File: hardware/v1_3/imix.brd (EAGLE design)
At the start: 87 x 102.5 mm, 154 parts, among them J2_3_5_AND_6 ARDUINO_R3NO_HOLES, SW1 TAC_SWITCHSMD, SW2 TAC_SWITCHSMD, U1 BQ2423X, U10 ISL29035, U11 FX0S8700CQ, U12 296-12686-1-ND, U13 SIP32401A, U14 SIP32401A, U15 SIP32401A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

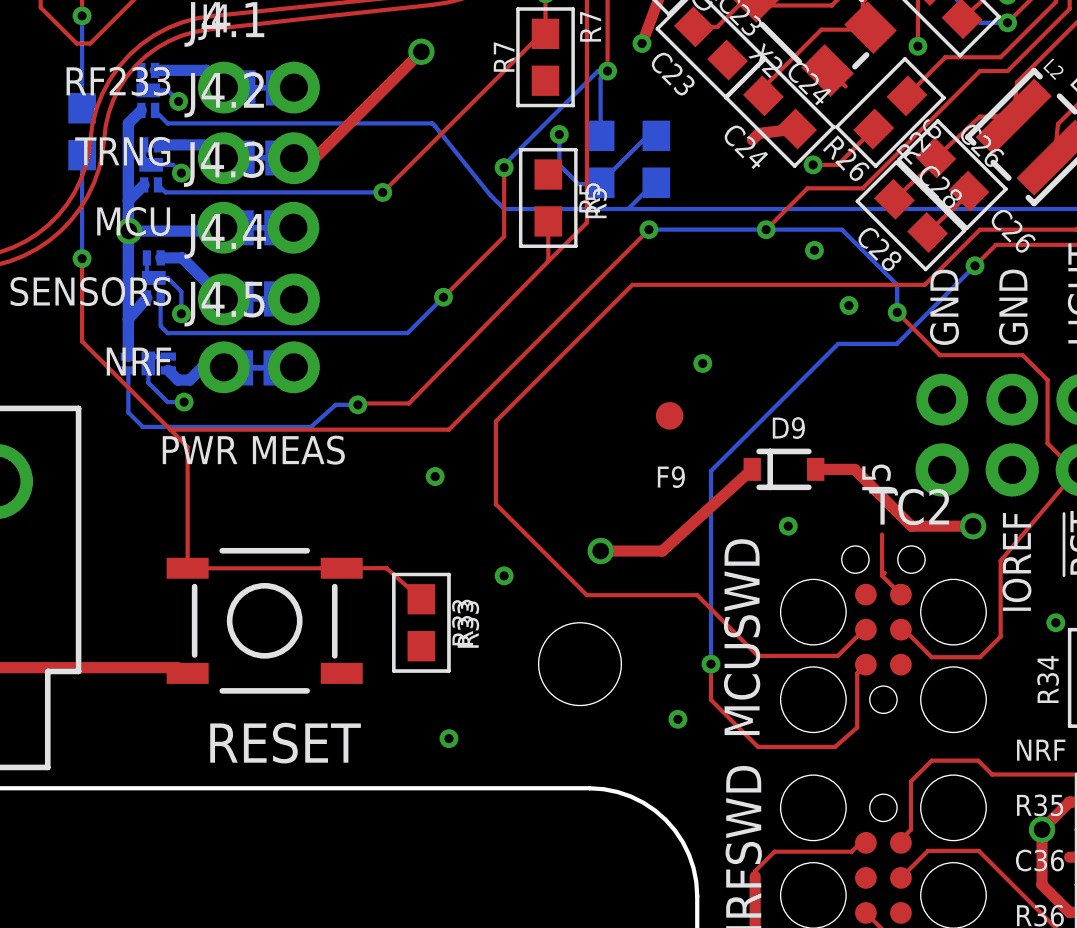
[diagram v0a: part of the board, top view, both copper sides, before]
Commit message: No airwires. Need to run DRC and generate documentation
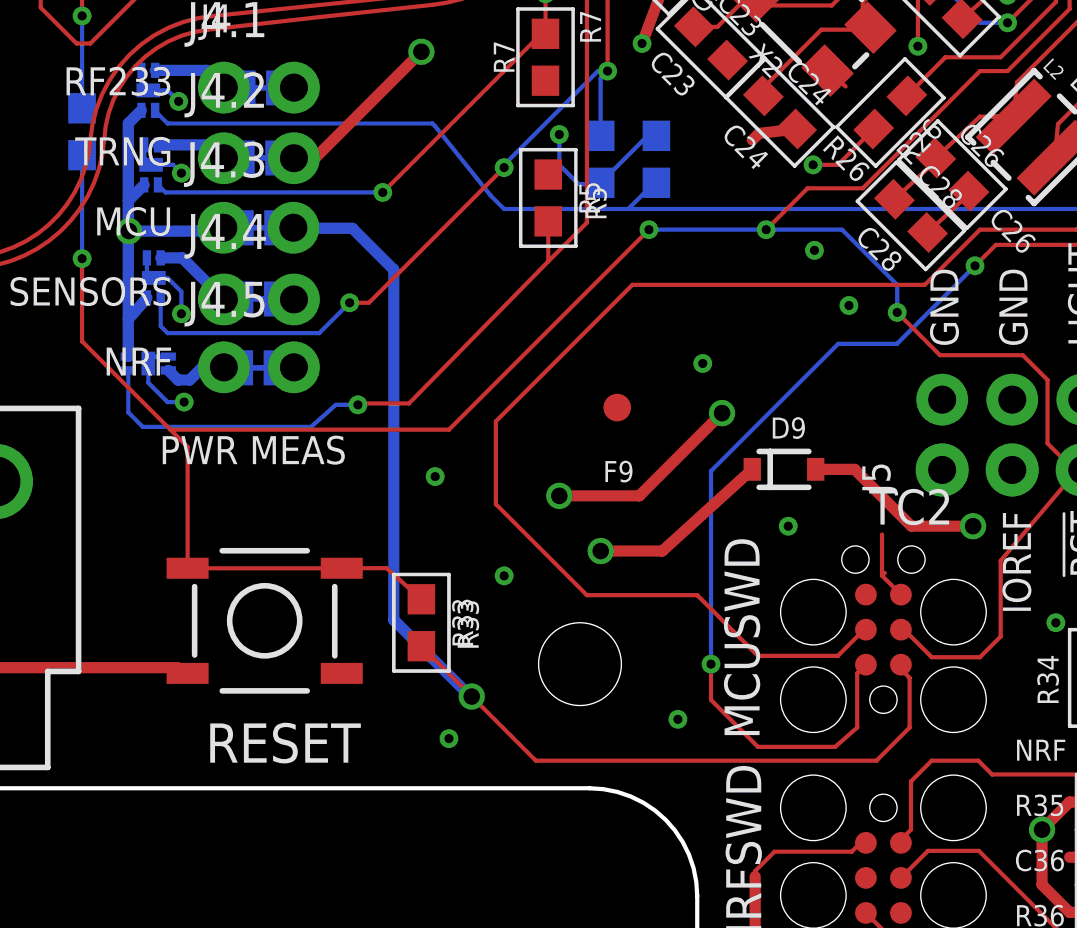
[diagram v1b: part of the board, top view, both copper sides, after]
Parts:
- moved F9 1.92 mm to (34.6, 13.8)
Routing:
- net VCC_MCU_3V3: track 71.0 -> 114.3 mm, vias 14 -> 15
- net VCC_3V3: track 39.4 -> 46.5 mm, vias 3 -> 5
- net SENSE_PWR_EN: track 148.8 -> 147.3 mm
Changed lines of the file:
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@@
 <wire x1="22.2" y1="13" x2="22.5" y2="13" width="0.1524" layer="22" style="shortdash"/>
 <wire x1="21.3" y1="13" x2="21.7" y2="13" width="0.1524" layer="22" style="shortdash"/>
-<text x="35.98" y="10.9" size="0.762" layer="21" font="vector" ratio="12">F9</text>
+<text x="34.08" y="11.1" size="0.762" layer="21" font="vector" ratio="12">F9</text>
 <text x="72.48" y="-9.1" size="0.762" layer="21" font="vector" ratio="12">F10</text>
 <text x="40.48" y="69.9" size="0.762" layer="21" font="vector" ratio="12">F7</text>
@@
 <element name="F7" library="imix" package="FIDUCIAL" value="FIDUCIAL" x="41" y="72.5"/>
 <element name="F8" library="imix" package="FIDUCIAL" value="FIDUCIAL" x="65.2" y="65.9"/>
-<element name="F9" library="imix" package="FIDUCIAL" value="FIDUCIAL" x="36.5" y="13.5"/>
+<element name="F9" library="imix" package="FIDUCIAL" value="FIDUCIAL" x="34.6" y="13.8"/>
 <element name="F10" library="imix" package="FIDUCIAL" value="FIDUCIAL" x="73.5" y="-6.5"/>
 <element name="R4" library="imix" package="0603-RES" value="10K" x="34" y="22.8" rot="MR90"/>
@@
 <wire x1="42.6" y1="22.6" x2="41.7" y2="22.6" width="0.1524" layer="1"/>
 <via x="41.7" y="22.6" extent="1-16" drill="0.3302"/>
-<wire x1="27.5" y1="5.15" x2="44.885" y2="4.48" width="0" layer="19" extent="1-1"/>
-<wire x1="22.86" y1="20.32" x2="27.5" y2="5.15" width="0" layer="19" extent="1-15"/>
+<wire x1="27.5" y1="5.15" x2="29.325" y2="3.325" width="0.1524" layer="1"/>
+<wire x1="29.325" y1="3.325" x2="31.65" y2="1" width="0.1524" layer="1"/>
+<wire x1="31.65" y1="1" x2="44" y2="1" width="0.1524" layer="1"/>
+<wire x1="44" y1="1" x2="45.2" y2="2.2" width="0.1524" layer="1"/>
+<wire x1="45.2" y1="2.2" x2="45.2" y2="4" width="0.1524" layer="1"/>
+<wire x1="45.2" y1="4" x2="44.885" y2="4.315" width="0.1524" layer="1"/>
+<wire x1="44.885" y1="4.315" x2="44.885" y2="4.48" width="0.1524" layer="1"/>
+<wire x1="22.86" y1="20.32" x2="22.88" y2="20.3" width="0.4064" layer="16"/>
+<wire x1="22.88" y1="20.3" x2="25" y2="20.3" width="0.4064" layer="16"/>
+<wire x1="25" y1="20.3" x2="26.5" y2="18.8" width="0.4064" layer="16"/>
+<wire x1="26.5" y1="18.8" x2="26.5" y2="6.1" width="0.4064" layer="16"/>
+<wire x1="26.5" y1="6.1" x2="29.275" y2="3.325" width="0.4064" layer="16"/>
+<wire x1="29.275" y1="3.325" x2="29.325" y2="3.325" width="0.4064" layer="16"/>
+<via x="29.325" y="3.325" extent="1-16" drill="0.6"/>
 </signal>
 <signal name="USART3_RTS">
@@
 <wire x1="75.1" y1="-5.2" x2="76.1" y2="-5.2" width="0.1524" layer="16"/>
 <wire x1="22.88" y1="17.72" x2="24.6" y2="16" width="0.4064" layer="15"/>
-<wire x1="24.6" y1="16" x2="33.8" y2="16" width="0.4064" layer="15"/>
-<wire x1="33.8" y1="16" x2="39.5" y2="10.3" width="0.4064" layer="15"/>
-<wire x1="39.5" y1="10.3" x2="45.2" y2="10.3" width="0.4064" layer="15"/>
+<wire x1="24.6" y1="16" x2="32.9" y2="16" width="0.4064" layer="15"/>
+<wire x1="32.9" y1="16" x2="38.6" y2="10.3" width="0.4064" layer="15"/>
+<wire x1="38.6" y1="10.3" x2="45.2" y2="10.3" width="0.4064" layer="15"/>
 <wire x1="45.2" y1="10.3" x2="47.4" y2="8.1" width="0.4064" layer="15"/>
 <wire x1="47.4" y1="8.1" x2="68.9" y2="8.1" width="0.4064" layer="15"/>
@@
 <contactref element="U18" pad="6"/>
 <contactref element="U18" pad="12"/>
-<wire x1="30.5" y1="22.5" x2="30.5" y2="20" width="0.1524" layer="1"/>
-<wire x1="30.5" y1="20" x2="28.3" y2="17.8" width="0.1524" layer="1"/>
 <wire x1="34.25" y1="26" x2="34" y2="25.75" width="0.1524" layer="16"/>
 <wire x1="34" y1="25.75" x2="34" y2="23.65" width="0.1524" layer="16"/>
-<wire x1="18.3" y1="16.5" x2="27" y2="16.5" width="0.1524" layer="16"/>
-<wire x1="27" y1="16.5" x2="28.3" y2="17.8" width="0.1524" layer="16"/>
-<via x="28.3" y="17.8" extent="1-16" drill="0.3302"/>
+<via x="24.9" y="17.6" extent="1-16" drill="0.3302"/>
 <wire x1="69" y1="43.5" x2="78.6" y2="43.5" width="0.1524" layer="16"/>
 <wire x1="78.6" y1="43.5" x2="79.6" y2="42.5" width="0.1524" layer="16"/>
@@
 <wire x1="18.05" y1="17.775" x2="18.05" y2="16.75" width="0.1524" layer="16"/>
 <wire x1="18.05" y1="16.75" x2="18.3" y2="16.5" width="0.1524" layer="16"/>
+<wire x1="24.9" y1="17.6" x2="23.8" y2="16.5" width="0.1524" layer="16"/>
+<wire x1="23.8" y1="16.5" x2="18.3" y2="16.5" width="0.1524" layer="16"/>
+<wire x1="30.5" y1="22.5" x2="25.6" y2="17.6" width="0.1524" layer="1"/>
+<wire x1="25.6" y1="17.6" x2="24.9" y2="17.6" width="0.1524" layer="1"/>
 </signal>
 <signal name="VCC_3V3" class="1">
@@
 <wire x1="16.875" y1="20.2" x2="16.9" y2="20.2" width="0.4064" layer="16"/>
 <via x="16.9" y="20.2" extent="1-16" drill="0.6"/>
-<wire x1="21.102" y1="20.32" x2="48.92" y2="11.54" width="0" layer="19" extent="16-16"/>
+<via x="38.4" y="13.6" extent="1-16" drill="0.6"/>
+<wire x1="38.4" y1="13.6" x2="35.4" y2="10.6" width="0.4064" layer="1"/>
+<wire x1="35.4" y1="10.6" x2="32.5" y2="10.6" width="0.4064" layer="1"/>
+<via x="32.5" y="10.6" extent="1-16" drill="0.6"/>
 </signal>
 <signal name="VCC_EXT_5V" class="1">

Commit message: Passes DRC
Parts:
- C47, C48: device imix:C0603 -> imix:C0603-NOSILK
- moved C6 0.55 mm to (54.4, 74.2)
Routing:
- net GND: track 234.7 -> 228.7 mm
- net VCC_3V3: track 46.5 -> 47.4 mm
- net N$4: track 10.3 -> 10.8 mm

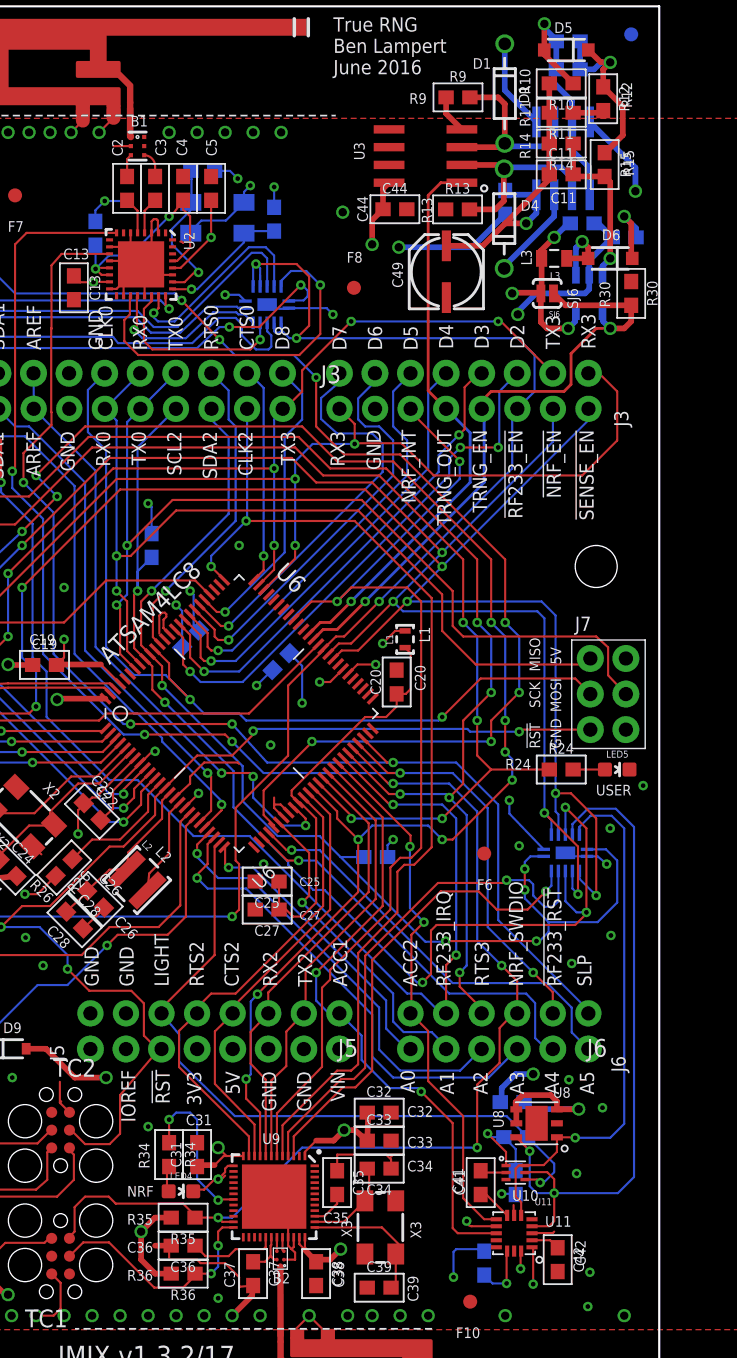
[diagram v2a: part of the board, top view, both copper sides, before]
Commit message: Rearranged analog pins according to #16
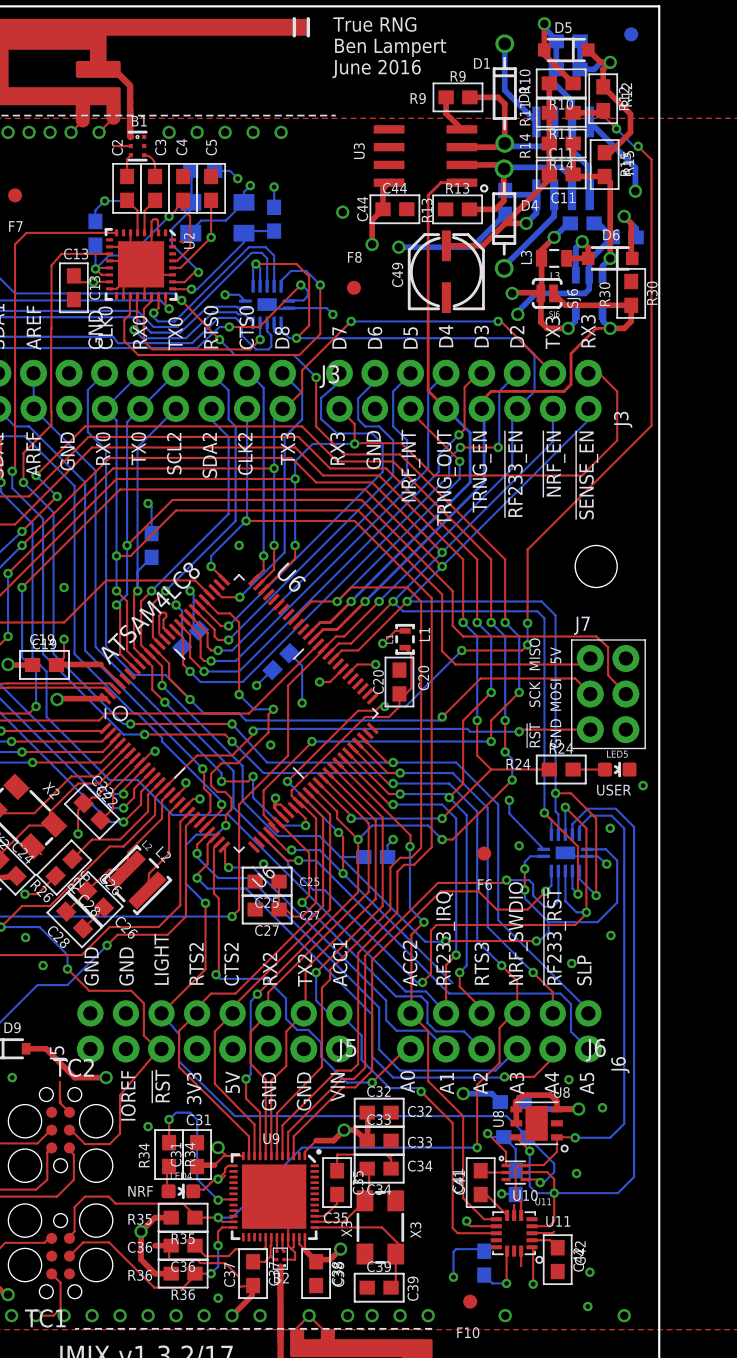
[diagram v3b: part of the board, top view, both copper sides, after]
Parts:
- moved C20 0.20 mm to (68.5, 37.8)
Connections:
- net ADCIFE0: now also U6.24; no longer U6.25
- net ADCIFE1: now also U6.25; no longer U6.31
- net ADCIFE2: now also U6.31; no longer U6.22
- net ADCIFE3: now also U6.22; no longer U6.23
- net ADCIFE4: now also U6.23; no longer U6.28
- net ADCIFE5: now also U6.28; no longer U6.29
- net GPIO8: now also U6.78; no longer U6.80
- net LIGHT_!INT: now also U6.80; no longer U6.24
- net VHIGHSAMPLE: now also U6.29
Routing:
- net VHIGHSAMPLE: track 2.21 -> 92.6 mm, vias 0 -> 10
- net LIGHT_!INT: track 50.7 -> 77.2 mm, vias 1 -> 5
- net ADCIFE4: track 28.4 -> 37.7 mm, vias 1 -> 2
- net ADCIFE0: track 21.1 -> 29.3 mm, vias 1 -> 2
- net ADCIFE2: track 31.2 -> 24.8 mm
- net GND: track 228.7 -> 225.4 mm, vias 94 -> 95
- net GPIO8: track 21.7 -> 20.5 mm
- net ADCIFE3: track 34.8 -> 33.7 mm
- net USART0_RX: track 64.3 -> 65.1 mm
- net AREF: track 44.2 -> 44.9 mm
- net ADCIFE1: track 22.7 -> 23.3 mm

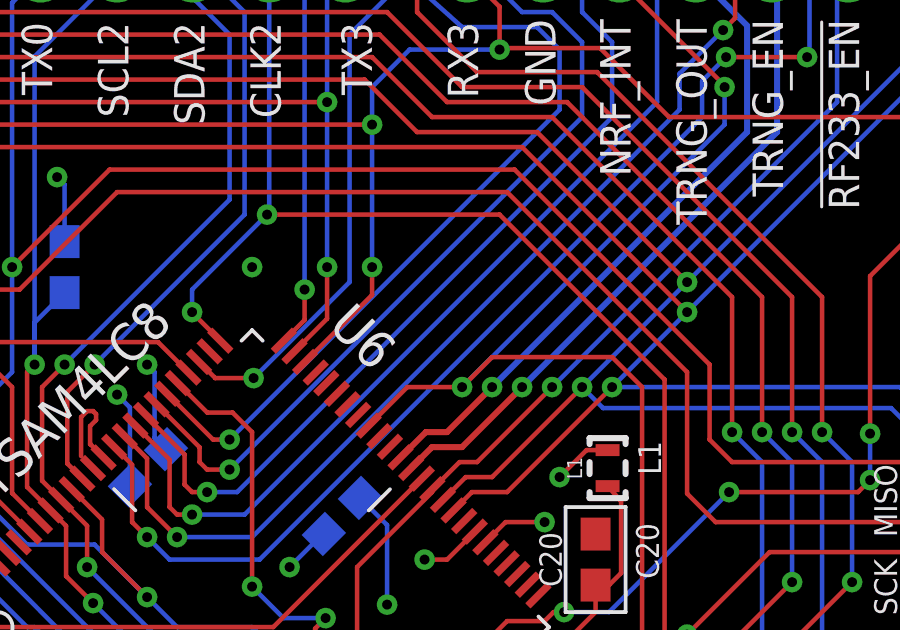
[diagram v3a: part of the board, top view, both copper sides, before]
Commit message: Fab/assembly documentation for v1.3
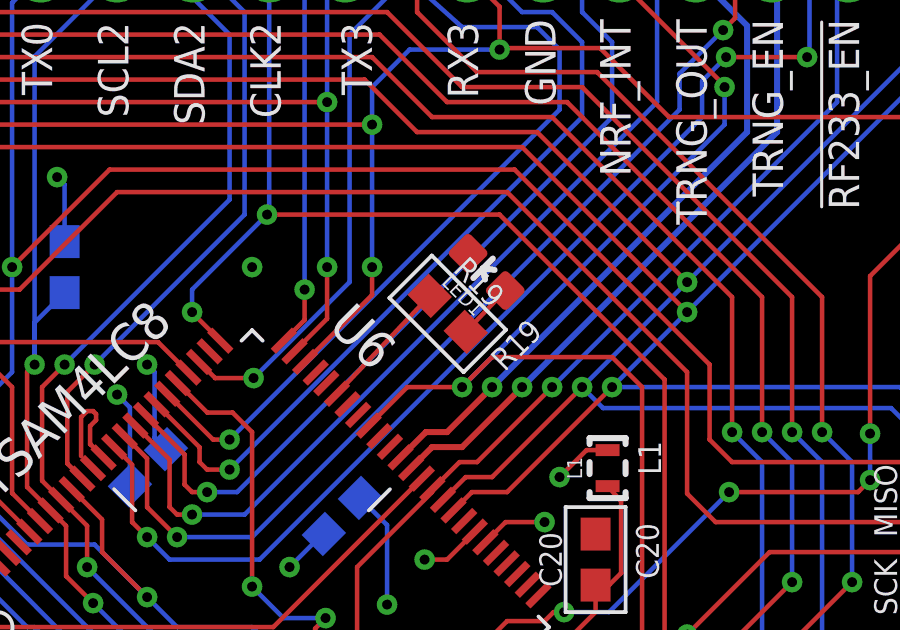
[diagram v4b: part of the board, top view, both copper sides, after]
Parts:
- added LED1: (no value), imix:LED-0603
- added R19: 1K, imix:0603-RES
- LED2, LED3, LED4, LED5: value BLUE -> (none)
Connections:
- new net KERNEL_LED: R19.1, U6.70
- new net N$14: LED1.A, R19.2
- net GND: now also LED1.C
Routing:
- net KERNEL_LED: track 0.00 -> 4.50 mm
- net N$14: track 0.00 -> 1.91 mm
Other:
- board text added: "R19"
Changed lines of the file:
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@@
 <text x="59.4" y="-5.2" size="0.762" layer="21" font="vector" ratio="12">B2</text>
 <wire x1="8" y1="7.3" x2="11" y2="7.3" width="0.4064" layer="21"/>
+<text x="65.42020625" y="43.985353125" size="0.762" layer="21" font="vector" ratio="12" rot="R45">R19</text>
 </plain>
 <attributes>
@@
 <element name="L1" library="imix" package="L0603" value="BLM18HE152SN1" x="69.25" y="40" rot="R90"/>
 <element name="L2" library="imix" package="L1212" value="22uH LQH3NPN220MJ0" x="49.715" y="23.605" rot="R315"/>
-<element name="LED2" library="imix" package="LED-0603" value="BLUE" x="3" y="44.5" smashed="yes" rot="R90">
+<element name="LED2" library="imix" package="LED-0603" value="" x="3" y="44.5" smashed="yes" rot="R90">
 <attribute name="PROD_ID" value="DIO-08575" x="3" y="44.5" size="1.778" layer="27" rot="R90" display="off"/>
 <attribute name="NAME" x="2.989" y="43.4015" size="0.5" layer="25" font="vector" ratio="12" rot="R180" align="center"/>
@@
 <attribute name="NAME" x="3.2" y="44.5" size="0.6" layer="51" font="vector" ratio="12" rot="R180" align="center"/>
 </element>
-<element name="LED4" library="imix" package="LED-0603" value="BLUE" x="52.846" y="1.38" rot="R270">
+<element name="LED4" library="imix" package="LED-0603" value="" x="52.846" y="1.38" rot="R270">
 <attribute name="PROD_ID" value="DIO-08575" x="52.846" y="1.38" size="1.778" layer="27" rot="R270" display="off"/>
 </element>
-<element name="LED5" library="imix" package="LED-0603" value="BLUE" x="84" y="31.5" rot="R270">
+<element name="LED5" library="imix" package="LED-0603" value="" x="84" y="31.5" rot="R270">
 <attribute name="PROD_ID" value="DIO-08575" x="84" y="31.5" size="1.778" layer="27" rot="R270" display="off"/>
 </element>
-<element name="LED3" library="imix" package="LED-0603" value="BLUE" x="3" y="41.5" smashed="yes" rot="R90">
+<element name="LED3" library="imix" package="LED-0603" value="" x="3" y="41.5" smashed="yes" rot="R90">
 <attribute name="PROD_ID" value="DIO-08575" x="3" y="41.5" size="1.778" layer="27" rot="R90" display="off"/>
 <attribute name="NAME" x="2.989" y="40.4015" size="0.5" layer="25" font="vector" ratio="12" rot="R180" align="center"/>
@@
 <attribute name="NAME" x="79.25" y="28.4" size="0.762" layer="22" font="vector" ratio="12" rot="MR180"/>
 </element>
+<element name="R19" library="imix" package="0603-RES" value="1K" x="63.5207125" y="45.941421875" rot="R315"/>
+<element name="LED1" library="imix" package="LED-0603" value="" x="64.820709375" y="47.3393375" rot="R45">
+<attribute name="PROD_ID" value="DIO-08575" x="64.820709375" y="47.3393375" size="1.778" layer="27" rot="R45" display="off"/>
+</element>
 </elements>
 <signals>
@@
 <wire x1="84.95" y1="77" x2="83.5" y2="75.55" width="0.4064" layer="1"/>
 <wire x1="83.5" y1="75.55" x2="83.1" y2="75.55" width="0.4064" layer="1"/>
+<contactref element="LED1" pad="C"/>
 </signal>
 <signal name="SWDIO/TMS">
@@
 <wire x1="55.55" y1="17.05" x2="55.35" y2="16.85" width="0.1524" layer="1"/>
 </signal>
+<signal name="N$14">
+<contactref element="LED1" pad="A"/>
+<contactref element="R19" pad="2"/>
+<wire x1="64.121753125" y1="45.340378125" x2="65.440840625" y2="46.719203125" width="0.1524" layer="1"/>
+</signal>
+<signal name="KERNEL_LED">
+<contactref element="R19" pad="1"/>
+<contactref element="U6" pad="70"/>
+<wire x1="59.828425" y1="43.278171875" x2="62.91966875" y2="46.5424625" width="0.1524" layer="1"/>
+</signal>
 </signals>
